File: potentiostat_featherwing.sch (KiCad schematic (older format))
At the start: 16 parts, among them J1 Screw_Terminal_01x03, P1 pin_array_3x1, U1 feather_wing, U2 LMP7721, U3 LMP7721, U4 LMP7721, U5 LMP7721

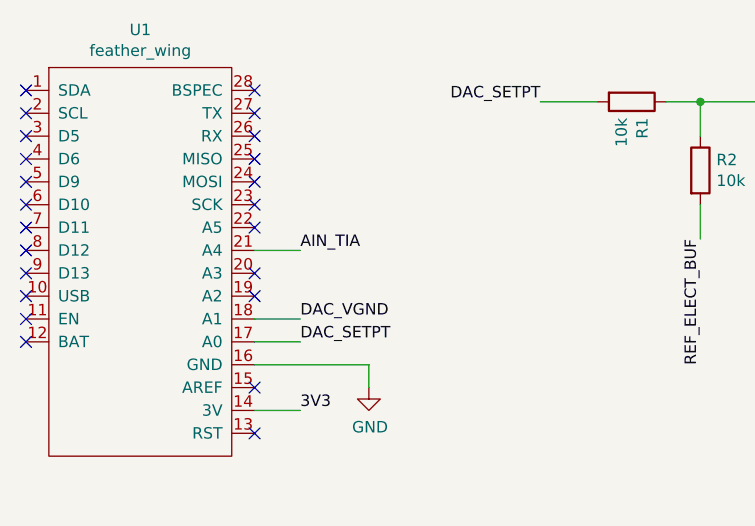
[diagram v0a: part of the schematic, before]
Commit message: Modified design so that ref elect (buffered) can be measured by analog input.
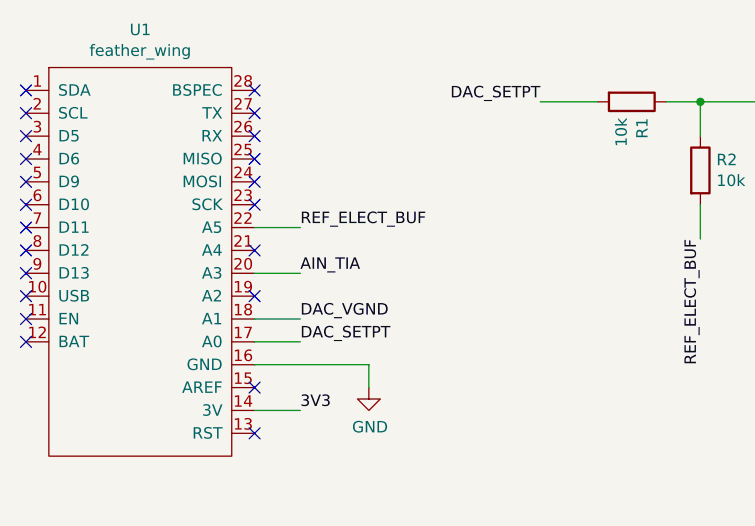
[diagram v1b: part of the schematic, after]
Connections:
- net AIN_TIA: now also U1.20 (A3); no longer U1.21 (A4)
- net REF_ELECT_BUF: now also U1.22 (A5)
- no-connect marks 33 -> 32
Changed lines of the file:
@@
 DAC_SETPT
 Wire Wire Line
-	2050 1600 2250 1600
-Text Label 2250 1600 0    50   ~ 0
+	2050 1700 2250 1700
+Text Label 2250 1700 0    50   ~ 0
 AIN_TIA
 Text Label 3300 950  2    50   ~ 0
@@
 NoConn ~ 2050 1300
 NoConn ~ 2050 1400
-NoConn ~ 2050 1500
-NoConn ~ 2050 1700
 NoConn ~ 2050 1800
 $Comp
@@
 Wire Wire Line
 	4850 4750 4850 5050
+NoConn ~ 2050 1600
+Wire Wire Line
+	2050 1500 2250 1500
+Text Label 2250 1500 0    50   ~ 0
+REF_ELECT_BUF
 $EndSCHEMATC
